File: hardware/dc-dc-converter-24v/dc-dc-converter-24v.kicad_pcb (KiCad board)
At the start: 4 copper layers, 100 x 100 mm, 56 parts, among them J1 12V, J2 24V, Q1 SQJA42EP, Q2 SQJA42EP, Q3 SQJA42EP, Q4 SQJA42EP, U1 LM5176

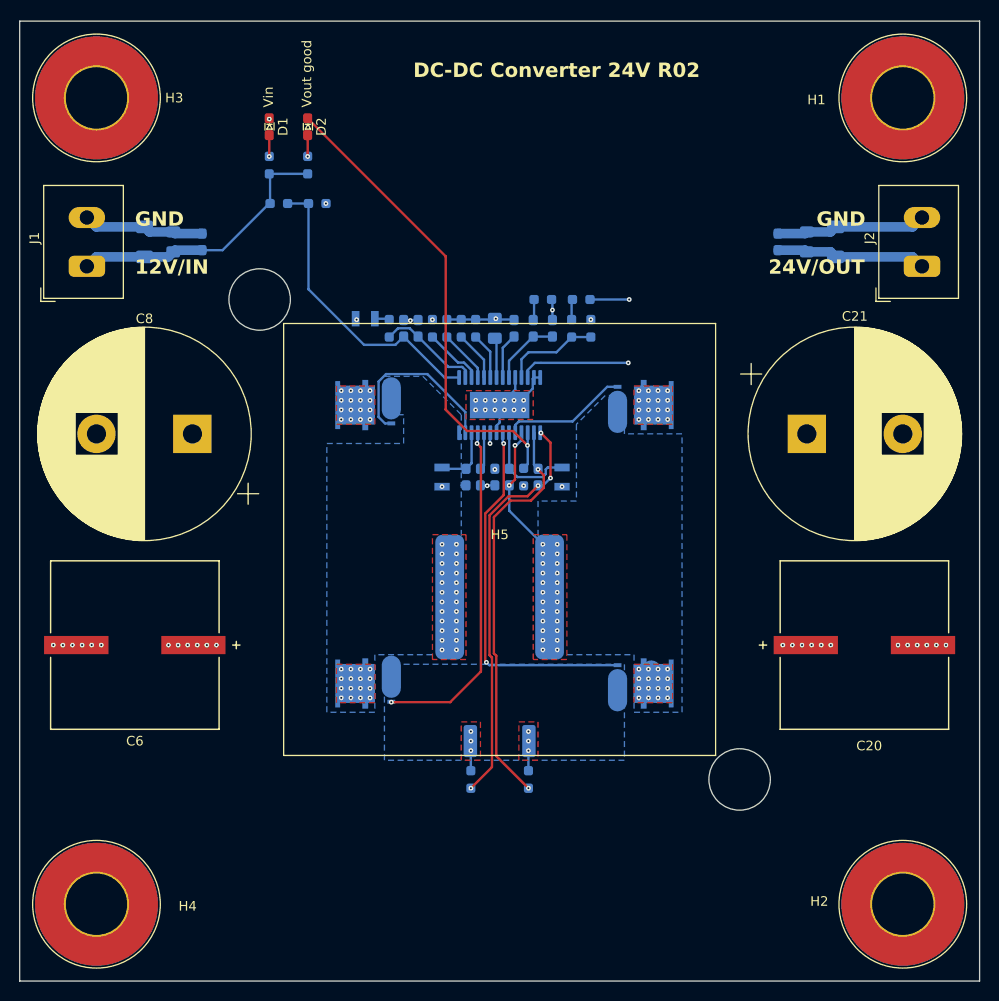
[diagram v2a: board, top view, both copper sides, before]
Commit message: create layout for DC-DC converter
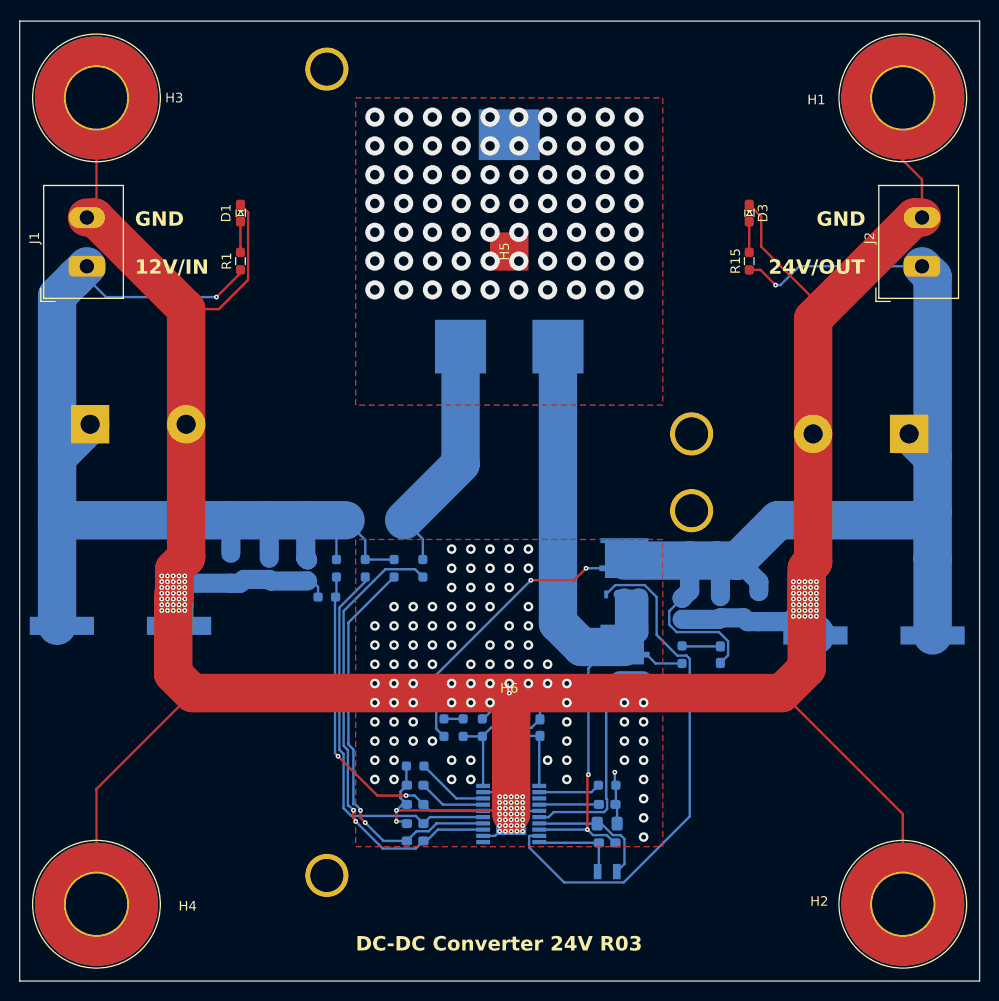
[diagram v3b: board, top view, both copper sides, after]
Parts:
- removed C21: 4700uF, benediktibk:CP_Radial_D22.0mm_P10.00mm_SnapIn
- removed D4, D5: BAT54WS, benediktibk:D_SOD-323
- removed Q3, Q4: SQJA42EP, benediktibk:SQJA42EPT1_GE3
- removed R16: 100Ohm, benediktibk:R_0603_1608Metric_Pad0.98x0.95mm_HandSolder
- removed R17: 4mOhm, benediktibk:R_2512_6332Metric_Pad1.40x3.35mm_HandSolder
- removed U1: LM5176, benediktibk:LM5176
- added H6: heatsink_HSB43-454515P, benediktibk:HSB43-454515P, F.Cu at (71.0, 90.0)
- added IC1: LM5122MHX_NOPB, benediktibk:SOP65P640X110-21N, B.Cu at (71.2, 102.6)
- C10: value 100nF -> 22nF
- C11: value 560pF -> 330pF
- C12: value 240pF -> 100nF; footprint benediktibk:C_0805_2012Metric_Pad1.18x1.45mm_HandSolder -> benediktibk:C_0603_1608Metric_Pad1.08x0.95mm_HandSolder
- C13: value 33nF -> 470nF
- C14: value 100nF -> 4.7uF; footprint benediktibk:C_0603_1608Metric_Pad1.08x0.95mm_HandSolder -> benediktibk:C_0805_2012Metric_Pad1.18x1.45mm_HandSolder
- C15: value 100nF -> 1uF
- C16: value 47pF -> 4.7uF; footprint benediktibk:C_0603_1608Metric_Pad1.08x0.95mm_HandSolder -> benediktibk:C_0805_2012Metric_Pad1.18x1.45mm_HandSolder
- C17: value 1uF -> 47uF; footprint benediktibk:C_0603_1608Metric_Pad1.08x0.95mm_HandSolder -> benediktibk:C_1206_3216Metric_Pad1.33x1.80mm_HandSolder
- C18: value 4.7uF -> 560pF; footprint benediktibk:C_0805_2012Metric_Pad1.18x1.45mm_HandSolder -> benediktibk:C_0603_1608Metric_Pad1.08x0.95mm_HandSolder
- C19: value 47uF -> 470uF; footprint benediktibk:C_1206_3216Metric_Pad1.33x1.80mm_HandSolder -> benediktibk:PCAP_16x16_5-ELECT_NCA-M
- C20: value 470uF -> 4700uF; footprint benediktibk:PCAP_16x16_5-ELECT_NCA-M -> benediktibk:CP_Radial_D22.0mm_P10.00mm_SnapIn; moved to B.Cu
- C3: value 100nF -> 470nF
- C5: value 100nF -> 470uF; footprint benediktibk:C_0603_1608Metric_Pad1.08x0.95mm_HandSolder -> benediktibk:PCAP_16x16_5-ELECT_NCA-M
- C6: value 470uF -> 100pF; footprint benediktibk:PCAP_16x16_5-ELECT_NCA-M -> benediktibk:C_0603_1608Metric_Pad1.08x0.95mm_HandSolder; moved to B.Cu
- C7: value 100nF -> 4700uF; footprint benediktibk:C_0603_1608Metric_Pad1.08x0.95mm_HandSolder -> benediktibk:CP_Radial_D22.0mm_P10.00mm_SnapIn
- C8: value 4700uF -> 100nF; footprint benediktibk:CP_Radial_D22.0mm_P10.00mm_SnapIn -> benediktibk:C_0603_1608Metric_Pad1.08x0.95mm_HandSolder; moved to B.Cu
- C9: value 1uF -> 100pF
- D2: value Vout good -> BAT54WS; footprint benediktibk:D_0603_1608Metric_Pad1.05x0.95mm_HandSolder -> benediktibk:D_SOD-323; moved to B.Cu
- D3: value BAT54WS -> Vout; footprint benediktibk:D_SOD-323 -> benediktibk:D_0603_1608Metric_Pad1.05x0.95mm_HandSolder; moved to F.Cu
- H5: value heatsink_ATS-CPX045045035-164-C2-R0 -> heatsink_HSB43-454515P; footprint benediktibk:heatsink_984-CPX04504-164C2R0 -> benediktibk:HSB43-454515P
- L1: value 2.5µH -> 7443641000B; footprint benediktibk:ETQP8 -> benediktibk:7443641000B
- R1: moved to F.Cu
- R10: value 10Ohm -> 1.5kOhm
- R11: value 10kOhm -> 2.7kOhm
- R12: value 10kOhm -> 68kOhm
- R13: value 20kOhm -> 50kOhm
- R14: value 270kOhm -> 8.2Ohm
- R15: value 100Ohm -> 1kOhm; moved to F.Cu
- R2: value 1kOhm -> 3.3Ohm
- R3: value 10kOhm -> 50kOhm
- R4: value 24kOhm -> 6.8kOhm
- R5: value 93.1kOhm -> 100Ohm
- R6: value 220kOhm -> 2mOhm; footprint benediktibk:R_0603_1608Metric_Pad0.98x0.95mm_HandSolder -> benediktibk:R_2512_6332Metric_Pad1.40x3.35mm_HandSolder
- R7: value 43kOhm -> 36kOhm
- R8: value 0Ohm -> 100Ohm
- R9: value 2kOhm -> 50kOhm
- moved D2 83.6 mm to (81.2, 108.6), turned to 0 degrees
- moved R7 59.5 mm to (61.2, 97.6), turned to 180 degrees
- moved R15 58.7 mm to (96.0, 45.0)
- moved C12 54.9 mm to (81.2, 105.6), turned to 0 degrees
- moved C5 51.4 mm to (30.5, 83.0), turned to 0 degrees
- moved R13 50.7 mm to (81.2, 99.6), turned to 0 degrees
- moved C13 50.2 mm to (81.2, 101.6), turned to 0 degrees
- moved R11 45.0 mm to (68.2, 93.6), turned to 90 degrees
- moved C18 43.9 mm to (93.0, 86.0), turned to -90 degrees
- moved C8 43.3 mm to (61.2, 99.6)
- moved C10 43.0 mm to (72.2, 93.6)
- moved R2 42.4 mm to (56.0, 77.0), turned to -90 degrees
- moved R10 42.3 mm to (66.2, 93.6)
- moved C11 41.6 mm to (74.2, 93.6)
- moved R9 41.6 mm to (64.2, 93.6), turned to 90 degrees
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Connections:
- C10 pad 1: Net-(U1-VIN) -> Net-(IC1-COMP)
- C10 pad 2: GND -> Net-(C10-Pad2)
- C11 pad 1: Net-(U1-COMP) -> Net-(IC1-COMP)
- C11 pad 2: GND -> Net-(IC1-FB)
- C12 pad 1: Net-(U1-SLOPE) -> Net-(D2-K)
- C12 pad 2: GND -> Net-(IC1-SW)
- C13 pad 1: Net-(U1-COMP) -> Net-(IC1-RES)
- C13 pad 2: Net-(C13-Pad2) -> GND
- C14 pad 1: Net-(D4-K) -> Net-(D2-A)
- C14 pad 2: Net-(Q1-S) -> GND
- C15 pad 1: Net-(D5-K) -> /Vout
- C15 pad 2: Net-(Q3-S) -> GND
- C16 pad 1: Net-(U1-CS) -> /Vout
- C16 pad 2: Net-(U1-CSG) -> GND
- C18 pad 1: /Vout -> Net-(C18-Pad1)
- C18 pad 2: GND -> /Vout
- C3 pad 1: Net-(U1-BIAS) -> Net-(IC1-VIN)
- C5 pad 1: Net-(U1-SS) -> /Vin
- C6 pad 1: /Vin -> Net-(IC1-UVLO)
- C7 pad 1: Net-(U1-EN/UVLO) -> /Vin
- C8 pad 1: /Vin -> Net-(IC1-SS)
- C9 pad 1: /Vcc -> Net-(IC1-CSP)
- C9 pad 2: GND -> Net-(IC1-CSN)
- D3 pad 1: Net-(D3-K) -> GND
- D3 pad 2: /Vin -> Net-(D3-A)
- L1 pad 1: Net-(Q1-S) -> Net-(IC1-SW)
- L1 pad 2: Net-(Q3-S) -> Net-(L1-Pad2)
- Q1 pad 1: Net-(Q1-S) -> GND
- Q1 pad 3: /Vin -> Net-(IC1-SW)
- Q2 pad 1: Net-(Q2-S) -> Net-(IC1-SW)
- Q2 pad 3: Net-(Q1-S) -> /Vout
- R10 pad 1: Net-(D3-K) -> Net-(R10-Pad1)
- R10 pad 2: Net-(U1-VIN) -> Net-(IC1-FB)
- R11 pad 1: Net-(C13-Pad2) -> Net-(IC1-FB)
- R12 pad 1: Net-(U1-FB) -> Net-(C10-Pad2)
- R12 pad 2: GND -> Net-(IC1-FB)
- R13 pad 1: /Vout -> Net-(IC1-SLOPE)
- R13 pad 2: Net-(R13-Pad2) -> GND
- R14 pad 1: Net-(R13-Pad2) -> Net-(IC1-SW)
- R14 pad 2: Net-(U1-FB) -> Net-(C18-Pad1)
- R15 pad 1: Net-(U1-CS) -> /Vout
- R15 pad 2: Net-(Q2-S) -> Net-(D3-A)
- R2 pad 2: Net-(D2-A) -> Net-(IC1-VIN)
- R3 pad 1: /Vcc -> /Vin
- R3 pad 2: Net-(D2-K) -> Net-(IC1-UVLO)
- R4 pad 1: Net-(U1-RT/SYNC) -> Net-(IC1-UVLO)
- R5 pad 1: GND -> /Vin
- R5 pad 2: Net-(U1-MODE) -> Net-(IC1-CSP)
- R6 pad 2: Net-(U1-EN/UVLO) -> Net-(L1-Pad2)
- R7 pad 1: Net-(U1-EN/UVLO) -> Net-(IC1-SYNCIN/RT)
- R8 pad 1: Net-(U1-DITH) -> Net-(L1-Pad2)
- R8 pad 2: GND -> Net-(IC1-CSN)
- R9 pad 1: /Vin -> /Vout
- R9 pad 2: Net-(U1-VISNS) -> Net-(R10-Pad1)
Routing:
- net GND: track 53.7 -> 378.2 mm, vias 34 -> 274
- net /Vout: track 31.3 -> 150.9 mm, vias 24 -> 3
- net /Vin: track 34.4 -> 118.0 mm, vias 24 -> 1
- net Net-(IC1-SW): track 0.00 -> 79.5 mm, vias 0 -> 2
- net Net-(IC1-CSN): track 0.00 -> 48.3 mm, vias 0 -> 2
- net Net-(U1-CS): track 42.5 -> 0.00 mm, vias 2 -> 0
- net Net-(U1-CSG): track 42.5 -> 0.00 mm, vias 4 -> 0
- net Net-(IC1-CSP): track 0.00 -> 42.2 mm, vias 0 -> 2
- net Net-(D2-K): track 50.3 -> 9.30 mm, vias 1 -> 0
- net Net-(IC1-VIN): track 0.00 -> 40.9 mm
- net Net-(Q4-G): track 38.6 -> 0.00 mm, vias 2 -> 0
- net Net-(IC1-UVLO): track 0.00 -> 36.3 mm, vias 0 -> 2
- net Net-(U1-EN/UVLO): track 31.3 -> 0.00 mm
- net Net-(L1-Pad2): track 0.00 -> 25.4 mm
- net Net-(IC1-HO): track 35.9 -> 54.3 mm, vias 2 -> 0
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- removed copper zone on In1.Cu, net /Vcc
- removed copper zone on F.Cu, net /Vin
- removed copper zone on In1.Cu, net /Vin
- removed copper zone on F.Cu, net /Vout
- removed copper zone on In1.Cu, net /Vout
- removed copper zone on In2.Cu, net GND
- removed copper zone on B.Cu, net Net-(Q1-S)
- removed copper zone on F.Cu, net Net-(Q1-S)
- removed copper zone on B.Cu, net Net-(Q2-S)
- removed copper zone on F.Cu, net Net-(Q2-S)
- removed copper zone on B.Cu, net Net-(Q3-S)
- removed copper zone on F.Cu, net Net-(Q3-S)
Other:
- copper layers 4 -> 2
- board text added: "DC-DC Converter 24V R03"
- board text removed: "DC-DC Converter 24V R02"
- board text removed: "Vin"
- board text removed: "Vout good"

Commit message: improve cooling for DC-DC converter
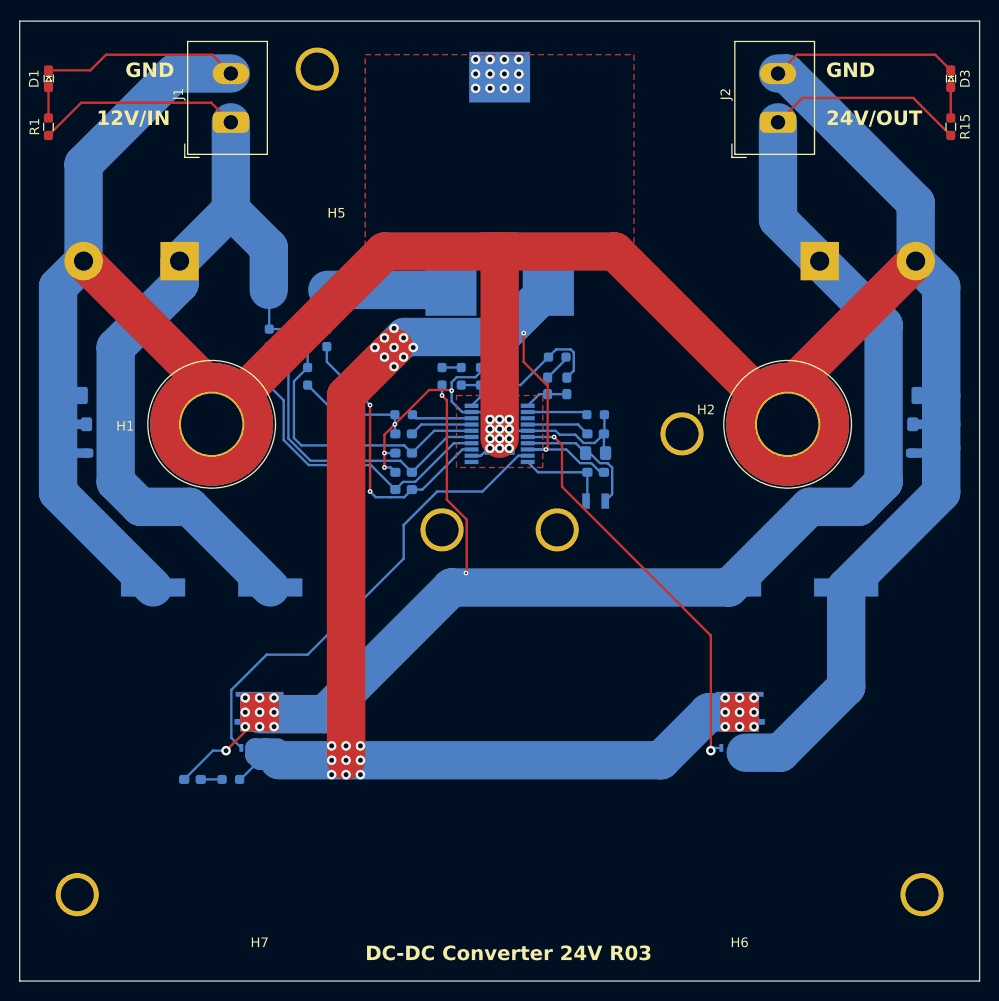
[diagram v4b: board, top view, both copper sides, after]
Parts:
- removed H3, H4: MountingHole_Pad_M6, benediktibk:MountingHole_6.4mm_M6_Pad_TopBottom
- added H7: heatsink_HSB43-454515P, benediktibk:HSB43-454515P, F.Cu at (45.0, 92.0)
- moved H1 79.6 mm to (40.0, 62.0)
- moved C18 56.5 mm to (38.0, 99.0), turned to 180 degrees
- moved H2 51.4 mm to (100.0, 62.0)
- moved R14 48.8 mm to (42.0, 99.0), turned to 180 degrees
- moved Q2 41.2 mm to (45.0, 93.0)
- moved IC1 39.6 mm to (70.0, 63.0)
- moved C12 38.6 mm to (80.0, 67.0)
- moved C13 38.6 mm to (80.0, 63.0)
- moved C14 38.6 mm to (80.0, 65.0)
- moved D2 38.6 mm to (80.0, 70.0)
- moved R13 38.6 mm to (80.0, 61.0)
- moved C9 36.6 mm to (60.0, 68.8)
- moved C3 36.6 mm to (60.0, 67.0)
- moved C6 36.6 mm to (60.0, 65.0)
- moved C8 36.6 mm to (60.0, 63.0)
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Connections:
- H6 pad PAD: GND -> Net-(IC1-SW)
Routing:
- net Net-(IC1-SW): track 79.5 -> 146.7 mm, vias 2 -> 29
- net GND: track 378.2 -> 411.5 mm, vias 274 -> 28
- net Net-(IC1-LO): track 20.8 -> 43.4 mm, vias 0 -> 2
- net /Vout: track 150.9 -> 169.5 mm, vias 3 -> 12
- net Net-(IC1-CSN): track 48.3 -> 29.8 mm
- net /Vin: track 118.0 -> 102.4 mm, vias 1 -> 0
- net Net-(IC1-VIN): track 40.9 -> 31.6 mm
- net Net-(L1-Pad2): track 25.4 -> 17.0 mm
- net Net-(IC1-CSP): track 42.2 -> 34.1 mm, vias 2 -> 0
- net Net-(IC1-UVLO): track 36.3 -> 30.2 mm, vias 2 -> 0
- net Net-(IC1-HO): track 54.3 -> 49.5 mm
- net Net-(IC1-FB): track 16.1 -> 18.9 mm
- net Net-(IC1-COMP): track 7.24 -> 4.58 mm
- net Net-(C18-Pad1): track 4.02 -> 2.23 mm
- net Net-(IC1-SYNCIN/RT): track 7.56 -> 6.32 mm
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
